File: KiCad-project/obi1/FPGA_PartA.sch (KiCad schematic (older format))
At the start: 14 parts, among them SW1 SW_Push, U3 XC6SLX16-FTG256, U4 OSC

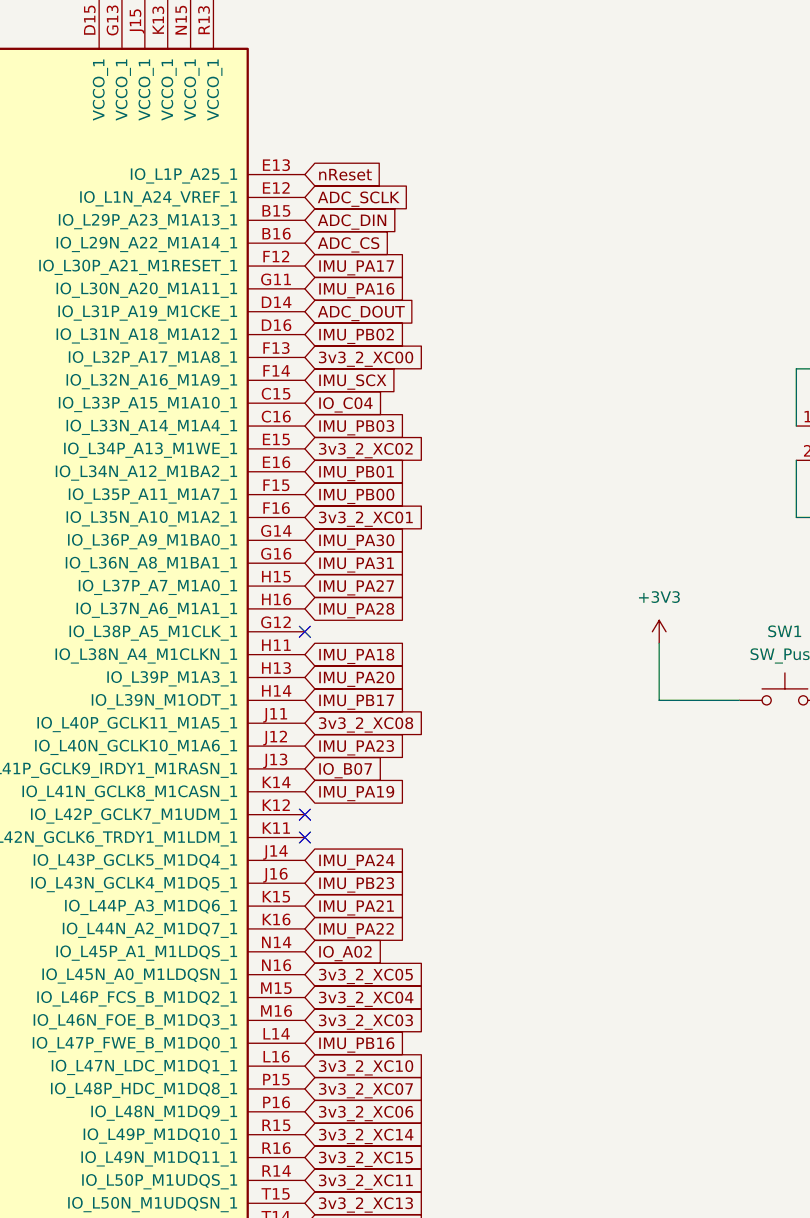
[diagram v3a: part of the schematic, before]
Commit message: IMU changed again, Final IMU= LSM6DSMTR, First Order to OSHPark
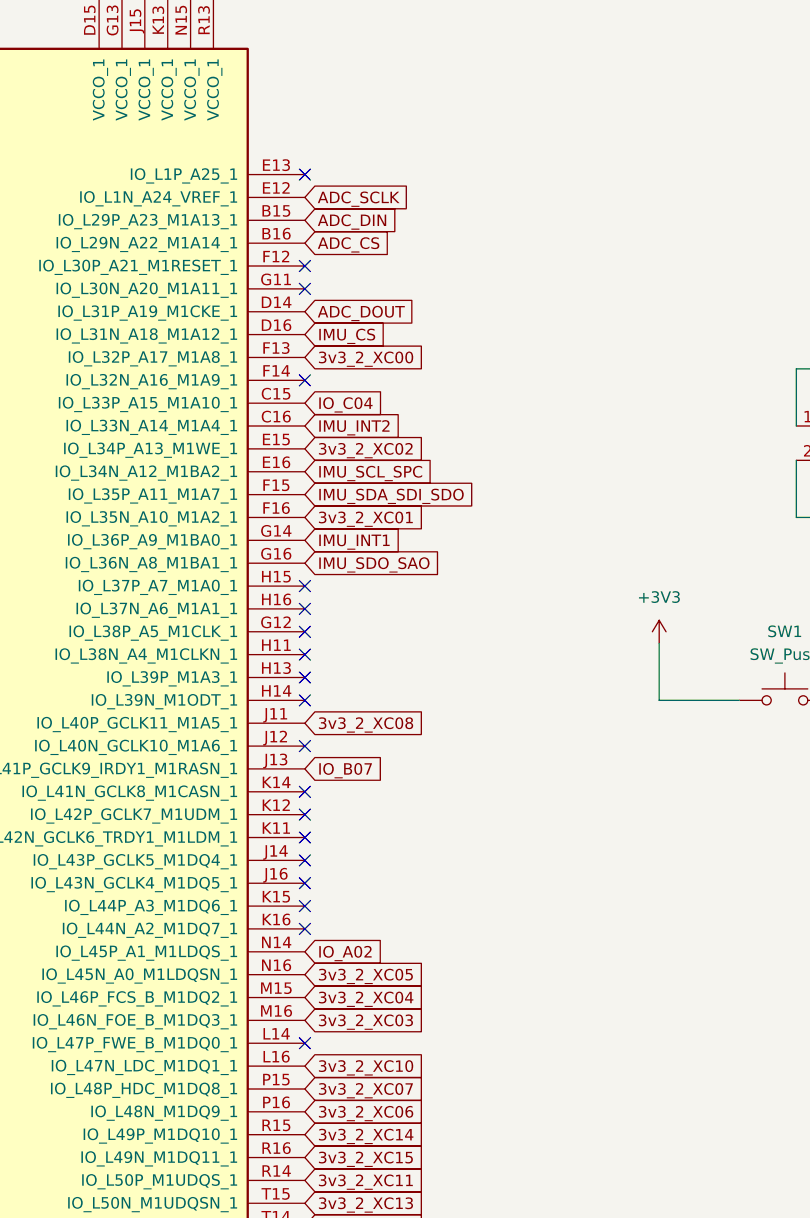
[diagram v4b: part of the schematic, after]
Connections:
- net IMU_PA16: no longer names the net of U3.G11 (IO_L30N_A20_M1A11_1)
- net IMU_PA17: no longer names the net of U3.F12 (IO_L30P_A21_M1RESET_1)
- net IMU_PA18: no longer names the net of U3.H11 (IO_L38N_A4_M1CLKN_1)
- net IMU_PA19: no longer names the net of U3.K14 (IO_L41N_GCLK8_M1CASN_1)
- net IMU_PA20: no longer names the net of U3.H13 (IO_L39P_M1A3_1)
- net IMU_PA21: no longer names the net of U3.K15 (IO_L44P_A3_M1DQ6_1)
- net IMU_PA22: no longer names the net of U3.K16 (IO_L44N_A2_M1DQ7_1)
- net IMU_PA23: no longer names the net of U3.J12 (IO_L40N_GCLK10_M1A6_1)
- net IMU_PA24: no longer names the net of U3.J14 (IO_L43P_GCLK5_M1DQ4_1)
- net IMU_PA27: no longer names the net of U3.H15 (IO_L37P_A7_M1A0_1)
- net IMU_PA28: no longer names the net of U3.H16 (IO_L37N_A6_M1A1_1)
- net IMU_PA30 renamed IMU_INT1
- net IMU_PA31 renamed IMU_SDO_SAO
- net IMU_PB00 renamed IMU_SDA_SDI_SDO
- net IMU_PB01 renamed IMU_SCL_SPC
- net IMU_PB02 renamed IMU_CS
- net IMU_PB03 renamed IMU_INT2
- net IMU_PB16: no longer names the net of U3.L14 (IO_L47P_FWE_B_M1DQ0_1)
- net IMU_PB17: no longer names the net of U3.H14 (IO_L39N_M1ODT_1)
- net IMU_PB23: no longer names the net of U3.J16 (IO_L43N_GCLK4_M1DQ5_1)
- net IMU_SCX: no longer names the net of U3.F14 (IO_L32N_A16_M1A9_1)
- net nReset: no longer names the net of U3.E13 (IO_L1P_A25_1)
- no-connect marks 15 -> 31
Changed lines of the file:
@@
 Connection ~ 9200 4000
 NoConn ~ 1550 3900
-Text GLabel 5550 3100 2    50   Input ~ 0
-IMU_PB00
-Text GLabel 5550 3000 2    50   Input ~ 0
-IMU_PB01
-Text GLabel 5550 2400 2    50   Input ~ 0
-IMU_PB02
-Text GLabel 5550 2800 2    50   Input ~ 0
-IMU_PB03
-Text GLabel 5550 5500 2    50   Input ~ 0
-IMU_PB16
-Text GLabel 5550 4000 2    50   Input ~ 0
-IMU_PB17
-Text GLabel 5550 4800 2    50   Input ~ 0
-IMU_PB23
-Text GLabel 5550 3400 2    50   Input ~ 0
-IMU_PA31
-Text GLabel 5550 3300 2    50   Input ~ 0
-IMU_PA30
-Text GLabel 5550 3600 2    50   Input ~ 0
-IMU_PA28
-Text GLabel 5550 3500 2    50   Input ~ 0
-IMU_PA27
-Text GLabel 5550 4700 2    50   Input ~ 0
-IMU_PA24
-Text GLabel 5550 4200 2    50   Input ~ 0
-IMU_PA23
-Text GLabel 5550 5000 2    50   Input ~ 0
-IMU_PA22
-Text GLabel 5550 4900 2    50   Input ~ 0
-IMU_PA21
-Text GLabel 5550 3900 2    50   Input ~ 0
-IMU_PA20
-Text GLabel 5550 4400 2    50   Input ~ 0
-IMU_PA19
-Text GLabel 5550 3800 2    50   Input ~ 0
-IMU_PA18
-Text GLabel 5550 2100 2    50   Input ~ 0
-IMU_PA17
-Text GLabel 5550 2200 2    50   Input ~ 0
-IMU_PA16
-Text GLabel 5550 1700 2    50   Input ~ 0
-nReset
 Wire Wire Line
 	7700 2800 7700 2550
@@
 Text GLabel 5550 2500 2    50   Input ~ 0
 3v3_2_XC00
-Text GLabel 5550 2600 2    50   Input ~ 0
-IMU_SCX
 Text GLabel 5550 6500 2    50   Input ~ 0
 XC_P12
@@
 Text GLabel 1550 1900 0    50   Input ~ 0
 RAM_A8
+Text GLabel 5550 3000 2    50   Input ~ 0
+IMU_SCL_SPC
+Text GLabel 5550 3100 2    50   Input ~ 0
+IMU_SDA_SDI_SDO
+Text GLabel 5550 3400 2    50   Input ~ 0
+IMU_SDO_SAO
+Text GLabel 5550 3300 2    50   Input ~ 0
+IMU_INT1
+Text GLabel 5550 2800 2    50   Input ~ 0
+IMU_INT2
+Text GLabel 5550 2400 2    50   Input ~ 0
+IMU_CS
+NoConn ~ 5550 1700
+NoConn ~ 5550 2100
+NoConn ~ 5550 2200
+NoConn ~ 5550 2600
+NoConn ~ 5550 3500
+NoConn ~ 5550 3600
+NoConn ~ 5550 3800
+NoConn ~ 5550 3900
+NoConn ~ 5550 4000
+NoConn ~ 5550 4200
+NoConn ~ 5550 4400
+NoConn ~ 5550 4700
+NoConn ~ 5550 4800
+NoConn ~ 5550 4900
+NoConn ~ 5550 5000
+NoConn ~ 5550 5500
 $EndSCHEMATC
